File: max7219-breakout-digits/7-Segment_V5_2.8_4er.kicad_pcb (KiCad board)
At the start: 2 copper layers, 51 x 12 mm, 5 parts, among them J1 Conn_02x08_Odd_Even, U1 HDSM-443B_CC_2Digit_7Segment_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, U2 HDSM-443B_CC_2Digit_7Segment_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

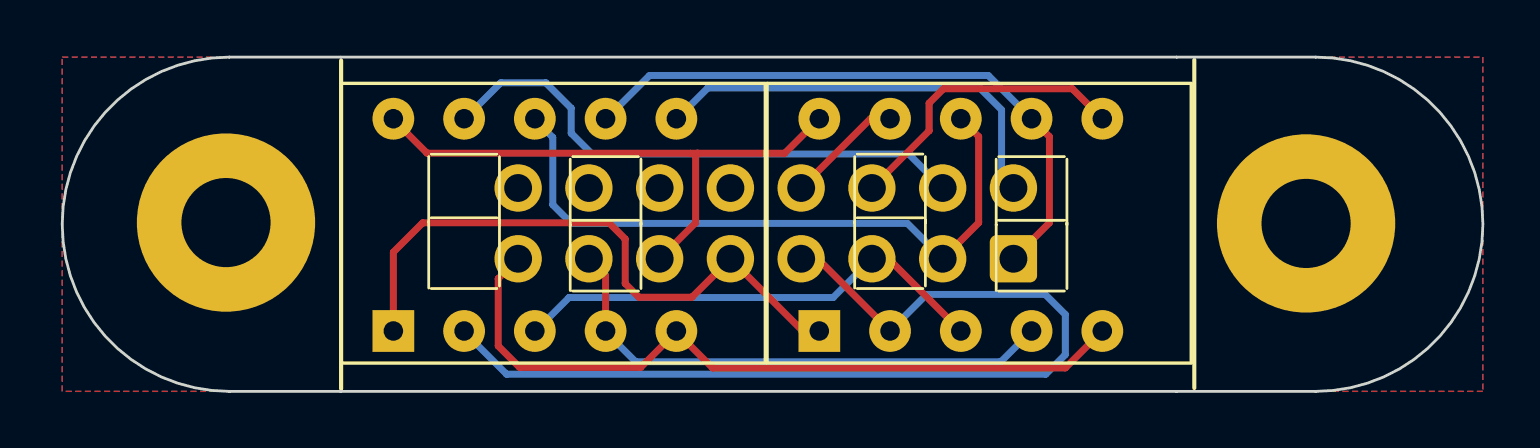
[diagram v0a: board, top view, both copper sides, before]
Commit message: center all mounting holes
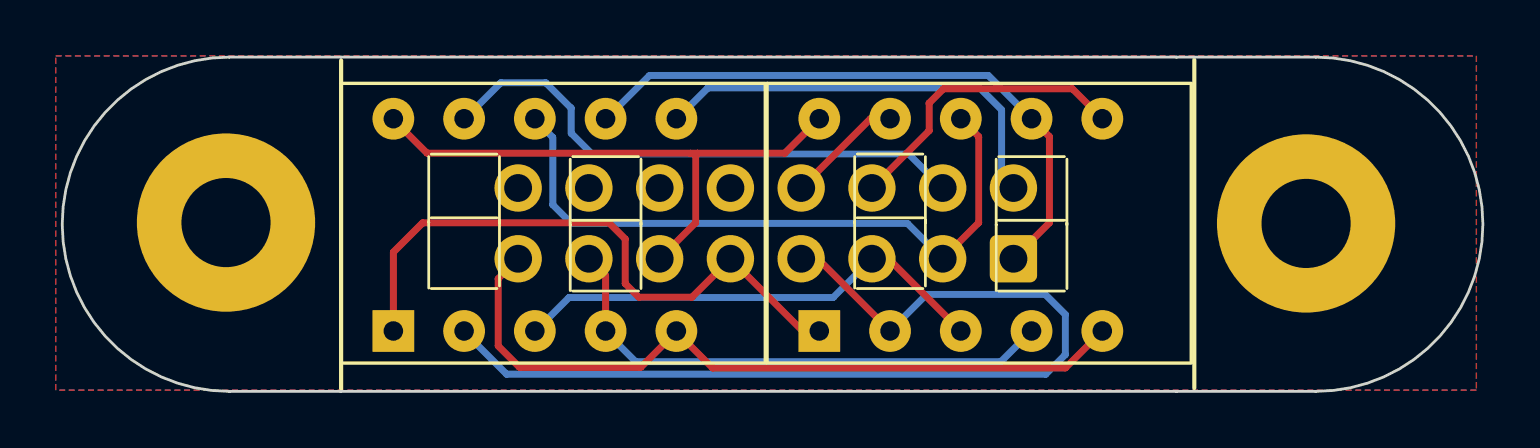
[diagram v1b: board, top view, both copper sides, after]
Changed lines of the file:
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@@
 			(type solid)
 		)
+		(locked yes)
 		(layer "Edge.Cuts")
 	)
@@
 			(type solid)
 		)
+		(locked yes)
 		(layer "Edge.Cuts")
 	)
@@
 			(type solid)
 		)
+		(locked yes)
 		(layer "Edge.Cuts")
 	)
@@
 			(type solid)
 		)
+		(locked yes)
 		(layer "Edge.Cuts")
 	)
@@
 			(type solid)
 		)
+		(locked yes)
 		(layer "Edge.Cuts")
 	)
@@
 			(type solid)
 		)
+		(locked yes)
 		(layer "Edge.Cuts")
 	)
@@
 			(type solid)
 		)
+		(locked yes)
 		(layer "Edge.Cuts")
 	)
@@
 			(type solid)
 		)
+		(locked yes)
 		(layer "Edge.Cuts")
 	)
@@
 		(polygon
 			(pts
-				(xy 121.615612 65.631212) (xy 70.615612 65.631212) (xy 70.615612 53.631212) (xy 121.615612 53.631212)
+				(xy 121.382112 65.586912) (xy 70.382112 65.586912) (xy 70.382112 53.586912) (xy 121.382112 53.586912)
 			)
 		)
 	)
+	(group ""
+		(members "52ccc360-486f-457b-abb0-4d26ccf28f0b" "d1533753-cca1-4ae0-9dbd-b73425c59b59")
+	)
+	(group ""
+		(locked yes)
+		(members "0f3207b0-7da8-4cc7-88c9-dbc35be7963c" "2e8141a5-6c04-4672-9cce-60f71f5df0a4"
+			"697602a5-614a-4354-9314-267df5fc4571" "896391fa-77aa-4617-be63-4c92c9128a73"
+			"89e45636-ec8b-4c1f-a910-cd710c78f8ab" "918fa49b-2224-43e2-9764-492f82d84f4c"
+			"b7bae9c8-4fed-4c69-a28c-182e2480bcdb" "e644f8a1-c356-4fc3-8857-cc821a08baea"
+		)
+	)
